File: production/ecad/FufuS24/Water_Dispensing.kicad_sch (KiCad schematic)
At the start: 8 parts, among them J12 691137710002, J13 5033950410, J8 691137710004, Q1 DMG2302UK-7

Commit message: Big layout push
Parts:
- added R25, R26, R27, R28: 10k, footprints:RESC2012X60N, symbol Device:R
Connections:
- net +5V: now also R25.1, R27.1
- net GNDREF: now also R26.2, R28.2
- net Watersense1_Mode renamed Watersense_Mode_2
- net Watersense_Mode_2: now also R27.2, R28.1
- net Watersense2_Mode renamed Watersense_Mode_1
- net Watersense_Mode_1: now also R25.2, R26.1
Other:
- moved on the sheet: J13, J8

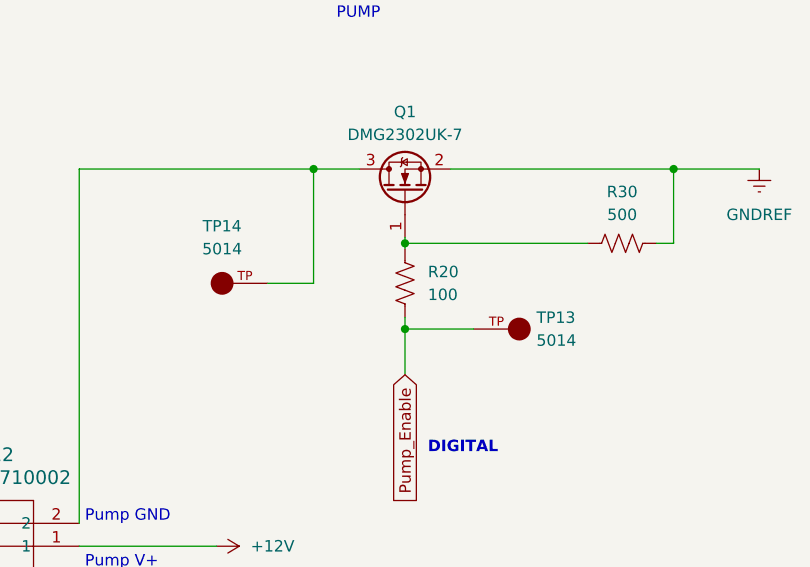
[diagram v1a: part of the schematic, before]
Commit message: major layout changes
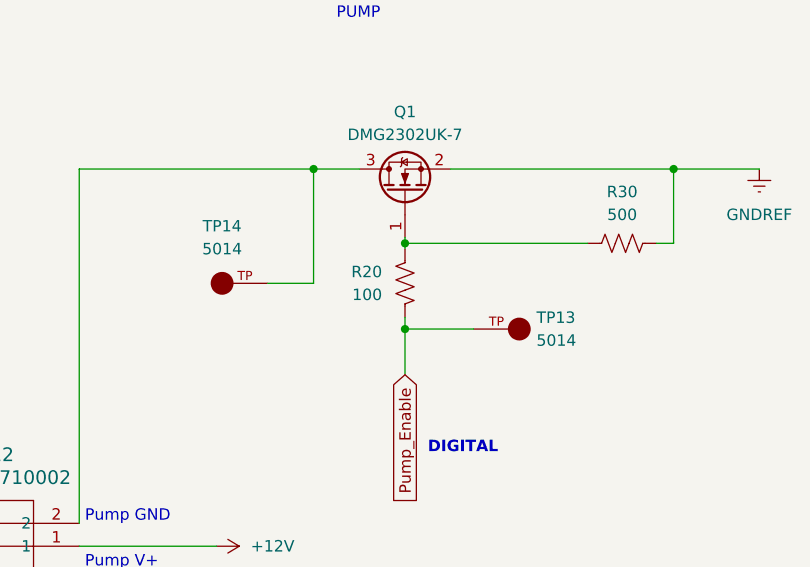
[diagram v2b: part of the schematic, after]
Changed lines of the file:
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@@
     )
   )
-  (symbol (lib_id "Device:R_US") (at 67.31 46.99 0) (unit 1)
-    (in_bom yes) (on_board yes) (dnp no) (fields_autoplaced)
-    (property "Reference" "R20" (at 69.85 45.72 0)
+  (symbol (lib_id "Device:R_US") (at 67.31 46.99 0) (mirror y) (unit 1)
+    (in_bom yes) (on_board yes) (dnp no)
+    (property "Reference" "R20" (at 64.77 45.72 0)
       (effects (font (size 1.27 1.27)) (justify left))
     )
-    (property "Value" "100" (at 69.85 48.26 0)
+    (property "Value" "100" (at 64.77 48.26 0)
       (effects (font (size 1.27 1.27)) (justify left))
     )
-    (property "Footprint" "footprints:RESC2012X60N" (at 68.326 47.244 90)
+    (property "Footprint" "footprints:RESC2012X60N" (at 66.294 47.244 90)
       (effects (font (size 1.27 1.27)) hide)
     )

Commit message: revised high speed signals
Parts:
- added TP17: 5014, footprints:TP_5014, symbol 5014:5014
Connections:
- net GNDREF: now also TP17.TP
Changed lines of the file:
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@@
   (junction (at 67.31 42.545) (diameter 0) (color 0 0 0 0)
   )
+  (junction (at 102.87 34.29) (diameter 0) (color 0 0 0 0)
+  )
   (junction (at 168.91 77.47) (diameter 0) (color 0 0 0 0)
   )
@@
     (stroke (width 0) (type default))
   )
+  (wire (pts (xy 102.87 34.29) (xy 106.68 34.29))
+    (stroke (width 0) (type default))
+  )
   (wire (pts (xy 160.02 72.39) (xy 168.91 72.39))
     (stroke (width 0) (type default))
@@
     (stroke (width 0) (type default))
   )
-  (wire (pts (xy 97.155 34.29) (xy 106.68 34.29))
+  (wire (pts (xy 97.155 34.29) (xy 102.87 34.29))
     (stroke (width 0) (type default))
   )
@@
     )
   )
+  (symbol (lib_id "5014:5014") (at 102.87 29.21 90) (unit 1)
+    (in_bom yes) (on_board yes) (dnp no) (fields_autoplaced)
+    (property "Reference" "TP17" (at 105.41 27.94 90)
+      (effects (font (size 1.27 1.27)) (justify right))
+    )
+    (property "Value" "5014" (at 105.41 30.48 90)
+      (effects (font (size 1.27 1.27)) (justify right))
+    )
+    (property "Footprint" "footprints:TP_5014" (at 102.87 29.21 0)
+      (effects (font (size 1.27 1.27)) (justify bottom) hide)
+    )
+    (property "Datasheet" "" (at 102.87 29.21 0)
+      (effects (font (size 1.27 1.27)) hide)
+    )
+    (property "MF" "Keystone" (at 102.87 29.21 0)
+      (effects (font (size 1.27 1.27)) (justify bottom) hide)
+    )
+    (property "MAXIMUM_PACKAGE_HEIGHT" "8.13 mm" (at 102.87 29.21 0)
+      (effects (font (size 1.27 1.27)) (justify bottom) hide)
+    )
+    (property "Package" "None" (at 102.87 29.21 0)
+      (effects (font (size 1.27 1.27)) (justify bottom) hide)
+    )
+    (property "Price" "None" (at 102.87 29.21 0)
+      (effects (font (size 1.27 1.27)) (justify bottom) hide)
+    )
+    (property "Check_prices" "https://www.snapeda.com/parts/5014/Keystone/view-part/?ref=eda" (at 102.87 29.21 0)
+      (effects (font (size 1.27 1.27)) (justify bottom) hide)
+    )
+    (property "STANDARD" "Manufacturer Recommendations" (at 102.87 29.21 0)
+      (effects (font (size 1.27 1.27)) (justify bottom) hide)
+    )
+    (property "PARTREV" "F" (at 102.87 29.21 0)
+      (effects (font (size 1.27 1.27)) (justify bottom) hide)
+    )
+    (property "SnapEDA_Link" "https://www.snapeda.com/parts/5014/Keystone/view-part/?ref=snap" (at 102.87 29.21 0)
+      (effects (font (size 1.27 1.27)) (justify bottom) hide)
+    )
+    (property "MP" "5014" (at 102.87 29.21 0)
+      (effects (font (size 1.27 1.27)) (justify bottom) hide)
+    )
+    (property "Purchase-URL" "https://www.snapeda.com/api/url_track_click_mouser/?unipart_id=500798&manufacturer=Keystone&part_name=5014&search_term=	 pc test point multipurpos" (at 102.87 29.21 0)
+      (effects (font (size 1.27 1.27)) (justify bottom) hide)
+    )
+    (property "Description" "\nTest Point MultiPurpose THM H .445 Nylon 46 Insulated Yel PhosBronze/Silver | Keystone Electronics 5014\n" (at 102.87 29.21 0)
+      (effects (font (size 1.27 1.27)) (justify bottom) hide)
+    )
+    (property "MANUFACTURER" "Keystone Electronics" (at 102.87 29.21 0)
+      (effects (font (size 1.27 1.27)) (justify bottom) hide)
+    )
+    (property "Availability" "In Stock" (at 102.87 29.21 0)
+      (effects (font (size 1.27 1.27)) (justify bottom) hide)
+    )
+    (property "SNAPEDA_PN" "5010" (at 102.87 29.21 0)
+      (effects (font (size 1.27 1.27)) (justify bottom) hide)
+    )
+    (pin "TP")
+    (instances
+      (project "FufuS24"
+        (path "/c4c3980b-c8c0-435e-abdc-bbed2349d7ac/57fb5dcd-e779-40d3-8741-57c7eee1ca58"
+          (reference "TP17") (unit 1)
+        )
+        (path "/c4c3980b-c8c0-435e-abdc-bbed2349d7ac/4167d6e6-5417-44cf-9a0c-baf8fab8b739"
+          (reference "TP24") (unit 1)
+        )
+      )
+    )
+  )

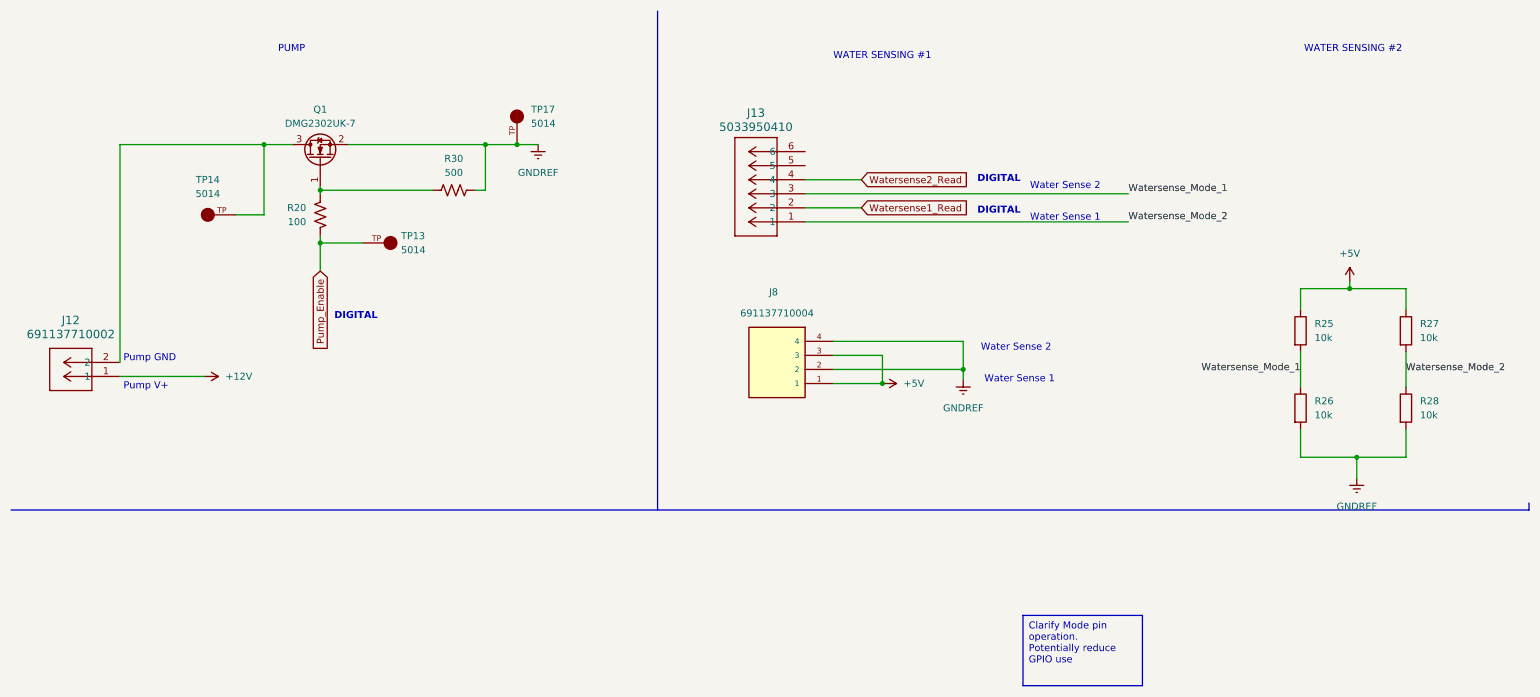
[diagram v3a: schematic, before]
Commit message: updated water sensor
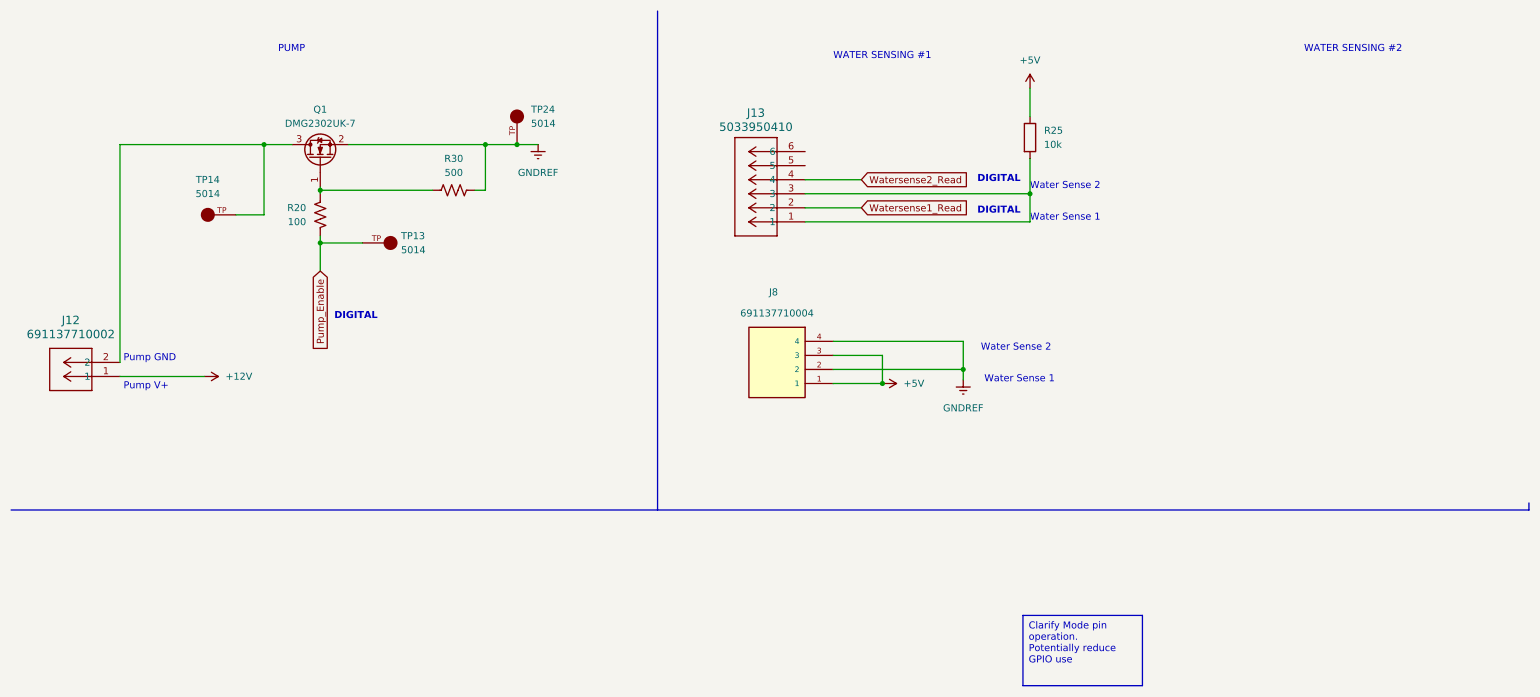
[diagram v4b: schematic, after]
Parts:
- removed R26, R27, R28: 10k, footprints:RESC2012X60N, symbol Device:R
- renumbered TP17 to TP24
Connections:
- net Watersense_Mode_2 is gone; now on an unnamed net: J13.1
- net Watersense_Mode_1: no longer names the net of J13.3, R25.2
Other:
- moved on the sheet: R25
